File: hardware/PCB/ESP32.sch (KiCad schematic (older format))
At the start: 24 parts, among them IC5 ESP32-D0WD-V3, U3 ESP32_Antenna, Y1 ABS05-32.768KHZ-T, Y2 ABM11AIG-40.000MHZ-4-1Z-T

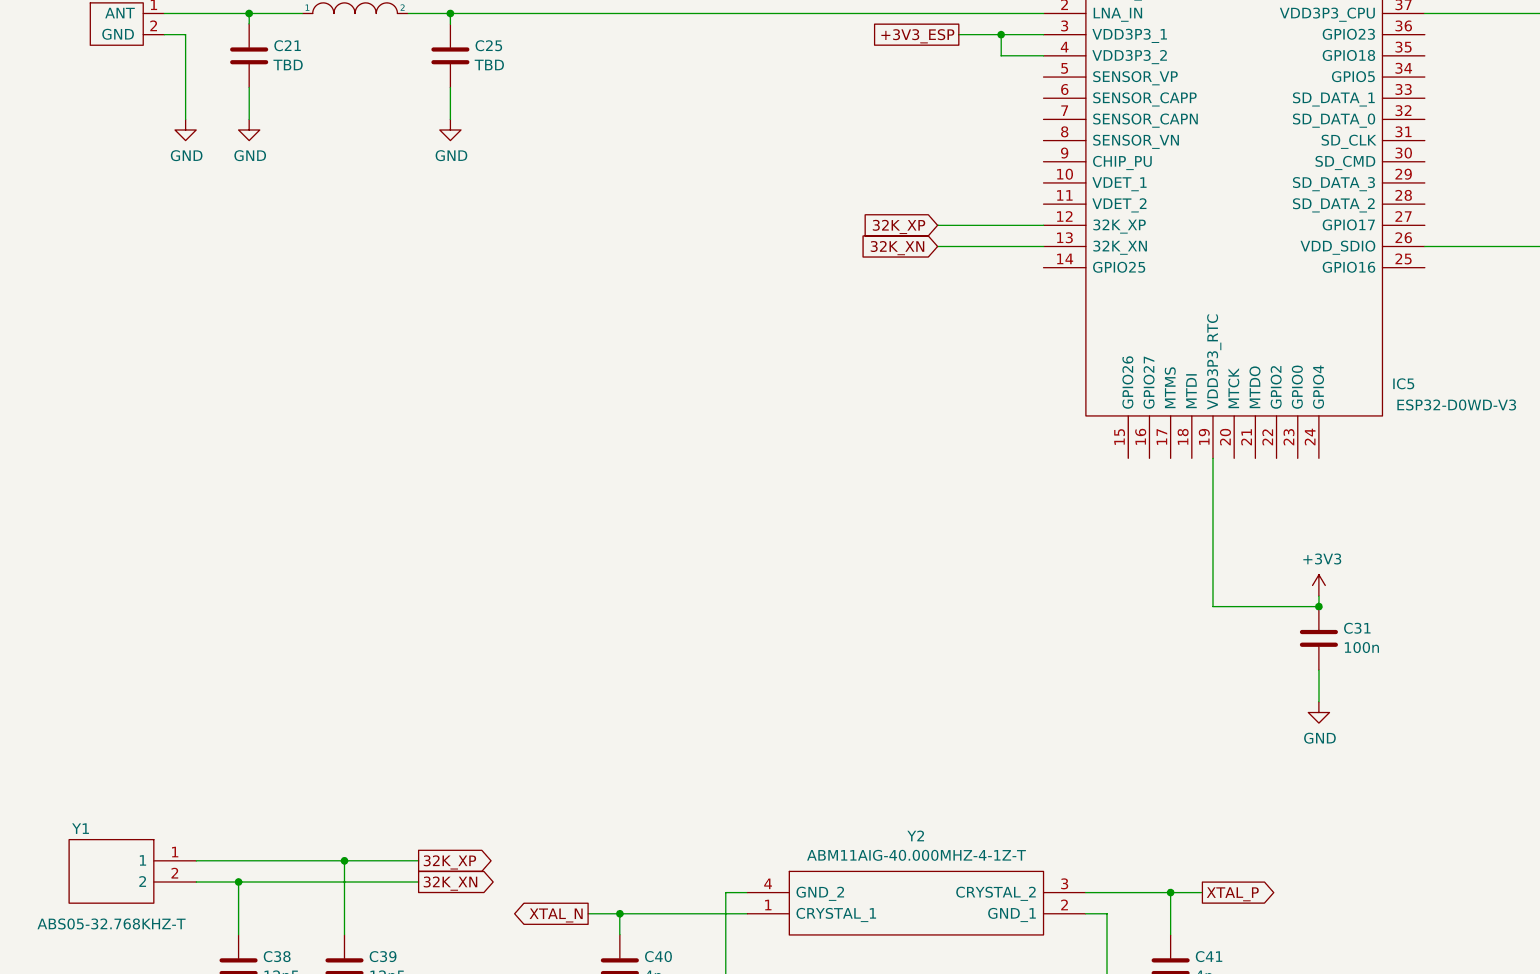
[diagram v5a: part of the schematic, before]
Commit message: add ESP32 bootloader circuit
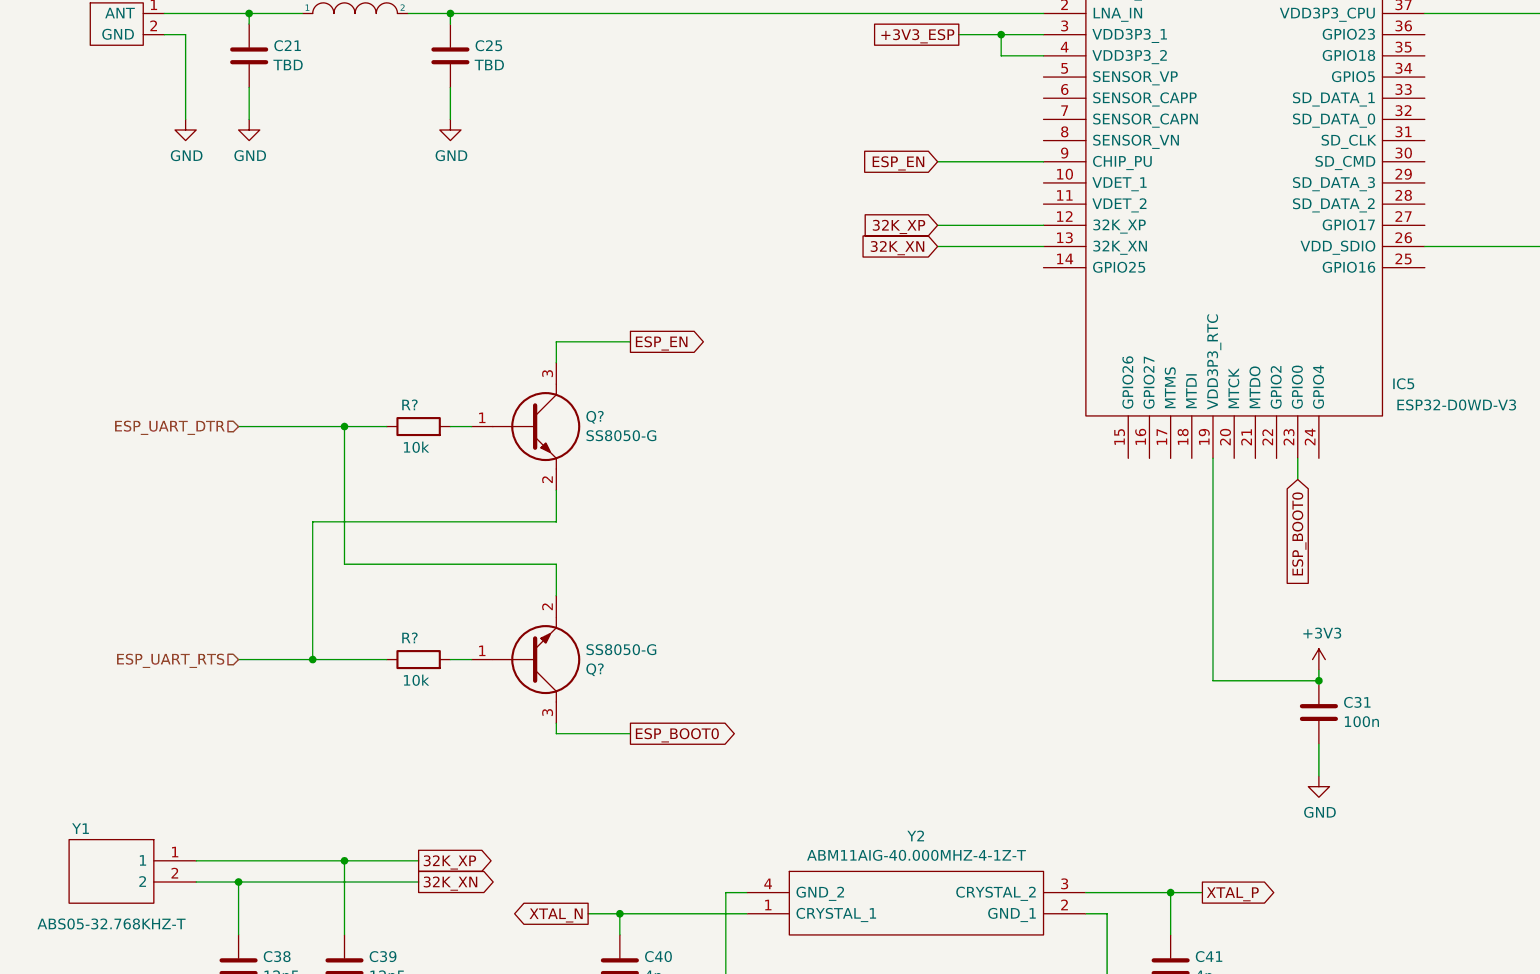
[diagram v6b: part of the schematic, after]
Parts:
- added Q? (x2): SS8050-G, SOT95P240X115-3N, symbol ProjectLibrary:SS8050-G
- added R? (x2): 10k, Resistor_SMD:R_0603_1608Metric, symbol Device:R
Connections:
- net ESP_BOOT0: now reaches IC5.23 (GPIO0)
- net ESP_BOOT0: now also Q?.3
- net ESP_EN: now reaches IC5.9 (CHIP_PU)
- net ESP_EN: now also Q?.3
- new net: Q?.1, R?.2 (x2)
- new net ESP_UART_DTR: Q?.2, R?.1
- new net ESP_UART_RTS: Q?.2, R?.1
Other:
- moved on the sheet: C31
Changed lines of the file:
@@
 L Device:C C?
 U 1 1 5FD526EC
-P 6600 5700
+P 6600 6050
 AR Path="/5FD526EC" Ref="C?"  Part="1"
 AR Path="/5FCFD0E2/5FD526EC" Ref="C31"  Part="1"
 AR Path="/5FE895CA/5FD526EC" Ref="C?"  Part="1"
-F 0 "C31" H 6715 5746 50  0000 L CNN
-F 1 "100n" H 6715 5655 50  0000 L CNN
-F 2 "Capacitor_SMD:C_0603_1608Metric" H 6638 5550 50  0001 C CNN
-F 3 "~" H 6600 5700 50  0001 C CNN
-	1    6600 5700
+F 0 "C31" H 6715 6096 50  0000 L CNN
+F 1 "100n" H 6715 6005 50  0000 L CNN
+F 2 "Capacitor_SMD:C_0603_1608Metric" H 6638 5900 50  0001 C CNN
+F 3 "~" H 6600 6050 50  0001 C CNN
+	1    6600 6050
 	1    0    0    -1
 $EndComp
@@
 L power:GND #PWR?
 U 1 1 5FD526F2
-P 6600 6000
+P 6600 6350
 AR Path="/5FD526F2" Ref="#PWR?"  Part="1"
 AR Path="/5FCFD0E2/5FD526F2" Ref="#PWR071"  Part="1"
 AR Path="/5FE895CA/5FD526F2" Ref="#PWR?"  Part="1"
-F 0 "#PWR071" H 6600 5750 50  0001 C CNN
-F 1 "GND" H 6605 5827 50  0000 C CNN
-F 2 "" H 6600 6000 50  0001 C CNN
-F 3 "" H 6600 6000 50  0001 C CNN
-	1    6600 6000
-	1    0    0    -1
-$EndComp
-Wire Wire Line
-	6600 5850 6600 6000
-Wire Wire Line
-	6100 4850 6100 5550
-Wire Wire Line
-	6100 5550 6600 5550
+F 0 "#PWR071" H 6600 6100 50  0001 C CNN
+F 1 "GND" H 6605 6177 50  0000 C CNN
+F 2 "" H 6600 6350 50  0001 C CNN
+F 3 "" H 6600 6350 50  0001 C CNN
+	1    6600 6350
+	1    0    0    -1
+$EndComp
+Wire Wire Line
+	6600 6200 6600 6350
+Wire Wire Line
+	6100 5900 6600 5900
 $Comp
 L ABS05-32.768KHZ-T:ABS05-32.768KHZ-T Y1
@@
 L power:+3V3 #PWR093
 U 1 1 5FF8D277
-P 6600 5500
+P 6600 5850
 AR Path="/5FCFD0E2/5FF8D277" Ref="#PWR093"  Part="1"
 AR Path="/5FE895CA/5FF8D277" Ref="#PWR?"  Part="1"
-F 0 "#PWR093" H 6600 5350 50  0001 C CNN
-F 1 "+3V3" H 6615 5673 50  0000 C CNN
-F 2 "" H 6600 5500 50  0001 C CNN
-F 3 "" H 6600 5500 50  0001 C CNN
-	1    6600 5500
-	1    0    0    -1
-$EndComp
-Wire Wire Line
-	6600 5500 6600 5550
-Connection ~ 6600 5550
+F 0 "#PWR093" H 6600 5700 50  0001 C CNN
+F 1 "+3V3" H 6615 6023 50  0000 C CNN
+F 2 "" H 6600 5850 50  0001 C CNN
+F 3 "" H 6600 5850 50  0001 C CNN
+	1    6600 5850
+	1    0    0    -1
+$EndComp
+Wire Wire Line
+	6600 5850 6600 5900
+Connection ~ 6600 5900
 $Comp
 L ProjectLibrary:ABM11AIG-40.000MHZ-4-1Z-T Y2
@@
 Wire Wire Line
 	6100 1800 6100 1950
+$Comp
+L ProjectLibrary:SS8050-G Q?
+U 1 1 5FFFFA03
+P 2600 4700
+F 0 "Q?" H 3138 4746 50  0000 L CNN
+F 1 "SS8050-G" H 3138 4655 50  0000 L CNN
+F 2 "SOT95P240X115-3N" H 3150 4550 50  0001 L CNN
+F 3 "http://www.comchiptech.com/admin/files/product/SS8050-G%20RevA181526.pdf" H 3150 4450 50  0001 L CNN
+F 4 "Bipolar Transistors - BJT NPN TRANSISTOR 1.5A 40V" H 3150 4350 50  0001 L CNN "Description"
+F 5 "1.15" H 3150 4250 50  0001 L CNN "Height"
+F 6 "750-SS8050-G" H 3150 4150 50  0001 L CNN "Mouser Part Number"
+F 7 "https://www.mouser.co.uk/ProductDetail/Comchip-Technology/SS8050-G/?qs=LLUE9lz1YbcHg%252BWLMAtcrQ%3D%3D" H 3150 4050 50  0001 L CNN "Mouser Price/Stock"
+F 8 "Comchip Technology" H 3150 3950 50  0001 L CNN "Manufacturer_Name"
+F 9 "SS8050-G" H 3150 3850 50  0001 L CNN "Manufacturer_Part_Number"
+	1    2600 4700
+	1    0    0    -1
+$EndComp
+$Comp
+L ProjectLibrary:SS8050-G Q?
+U 1 1 60008ECC
+P 2600 5800
+F 0 "Q?" H 3138 5846 50  0000 L CNN
+F 1 "SS8050-G" H 3138 5755 50  0000 L CNN
+F 2 "SOT95P240X115-3N" H 3150 5650 50  0001 L CNN
+F 3 "http://www.comchiptech.com/admin/files/product/SS8050-G%20RevA181526.pdf" H 3150 5550 50  0001 L CNN
+F 4 "Bipolar Transistors - BJT NPN TRANSISTOR 1.5A 40V" H 3150 5450 50  0001 L CNN "Description"
+F 5 "1.15" H 3150 5350 50  0001 L CNN "Height"
+F 6 "750-SS8050-G" H 3150 5250 50  0001 L CNN "Mouser Part Number"
+F 7 "https://www.mouser.co.uk/ProductDetail/Comchip-Technology/SS8050-G/?qs=LLUE9lz1YbcHg%252BWLMAtcrQ%3D%3D" H 3150 5150 50  0001 L CNN "Mouser Price/Stock"
+F 8 "Comchip Technology" H 3150 5050 50  0001 L CNN "Manufacturer_Name"
+F 9 "SS8050-G" H 3150 4950 50  0001 L CNN "Manufacturer_Part_Number"
+	1    2600 5800
+	1    0    0    1
+$EndComp
+$Comp
+L Device:R R?
+U 1 1 6000F441
+P 2350 4700
+AR Path="/6000F441" Ref="R?"  Part="1"
+AR Path="/5FCFD0E2/6000F441" Ref="R?"  Part="1"
+AR Path="/5FE895CA/6000F441" Ref="R?"  Part="1"
+F 0 "R?" V 2450 4700 50  0000 L CNN
+F 1 "10k" V 2250 4650 50  0000 L CNN
+F 2 "Resistor_SMD:R_0603_1608Metric" V 2280 4700 50  0001 C CNN
+F 3 "~" H 2350 4700 50  0001 C CNN
+	1    2350 4700
+	0    -1   -1   0
+$EndComp
+$Comp
+L Device:R R?
+U 1 1 60013917
+P 2350 5800
+AR Path="/60013917" Ref="R?"  Part="1"
+AR Path="/5FCFD0E2/60013917" Ref="R?"  Part="1"
+AR Path="/5FE895CA/60013917" Ref="R?"  Part="1"
+F 0 "R?" V 2450 5800 50  0000 L CNN
+F 1 "10k" V 2250 5750 50  0000 L CNN
+F 2 "Resistor_SMD:R_0603_1608Metric" V 2280 5800 50  0001 C CNN
+F 3 "~" H 2350 5800 50  0001 C CNN
+	1    2350 5800
+	0    -1   -1   0
+$EndComp
+Text HLabel 1500 5800 0    50   Input ~ 0
+ESP_UART_RTS
+Text HLabel 1500 4700 0    50   Input ~ 0
+ESP_UART_DTR
+Wire Wire Line
+	2500 4700 2600 4700
+Wire Wire Line
+	2500 5800 2600 5800
+Wire Wire Line
+	1500 4700 2000 4700
+Wire Wire Line
+	1500 5800 1850 5800
+Wire Wire Line
+	3000 5500 3000 5350
+Wire Wire Line
+	3000 5350 2000 5350
+Wire Wire Line
+	2000 5350 2000 4700
+Connection ~ 2000 4700
+Wire Wire Line
+	2000 4700 2200 4700
+Wire Wire Line
+	3000 5000 3000 5150
+Wire Wire Line
+	3000 5150 1850 5150
+Wire Wire Line
+	1850 5150 1850 5800
+Connection ~ 1850 5800
+Wire Wire Line
+	1850 5800 2200 5800
+Text GLabel 3350 4300 2    50   Output ~ 0
+ESP_EN
+Wire Wire Line
+	3000 4400 3000 4300
+Wire Wire Line
+	3000 4300 3350 4300
+Text GLabel 3350 6150 2    50   Output ~ 0
+ESP_BOOT0
+Wire Wire Line
+	3350 6150 3000 6150
+Wire Wire Line
+	3000 6150 3000 6100
+Text GLabel 6500 4950 3    50   Input ~ 0
+ESP_BOOT0
+Wire Wire Line
+	6100 4850 6100 5900
+Wire Wire Line
+	6500 4950 6500 4850
+Text GLabel 4800 3450 0    50   Input ~ 0
+ESP_EN
+Wire Wire Line
+	4800 3450 5300 3450
 $EndSCHEMATC

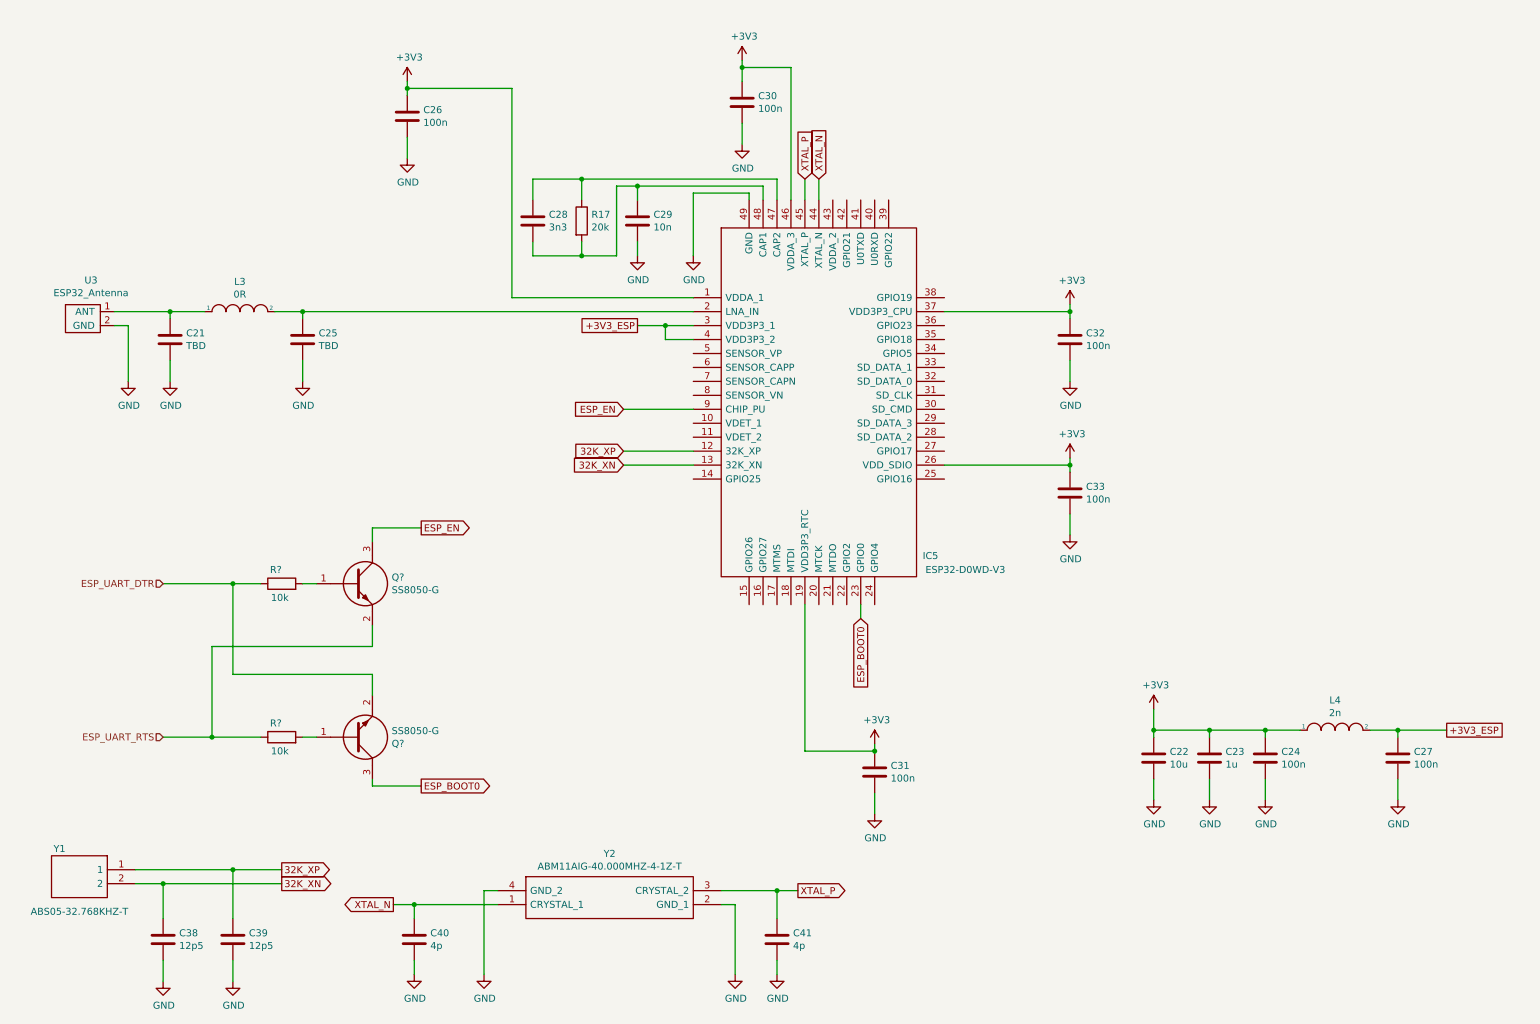
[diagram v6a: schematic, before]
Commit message: add enable and boot0 buttons
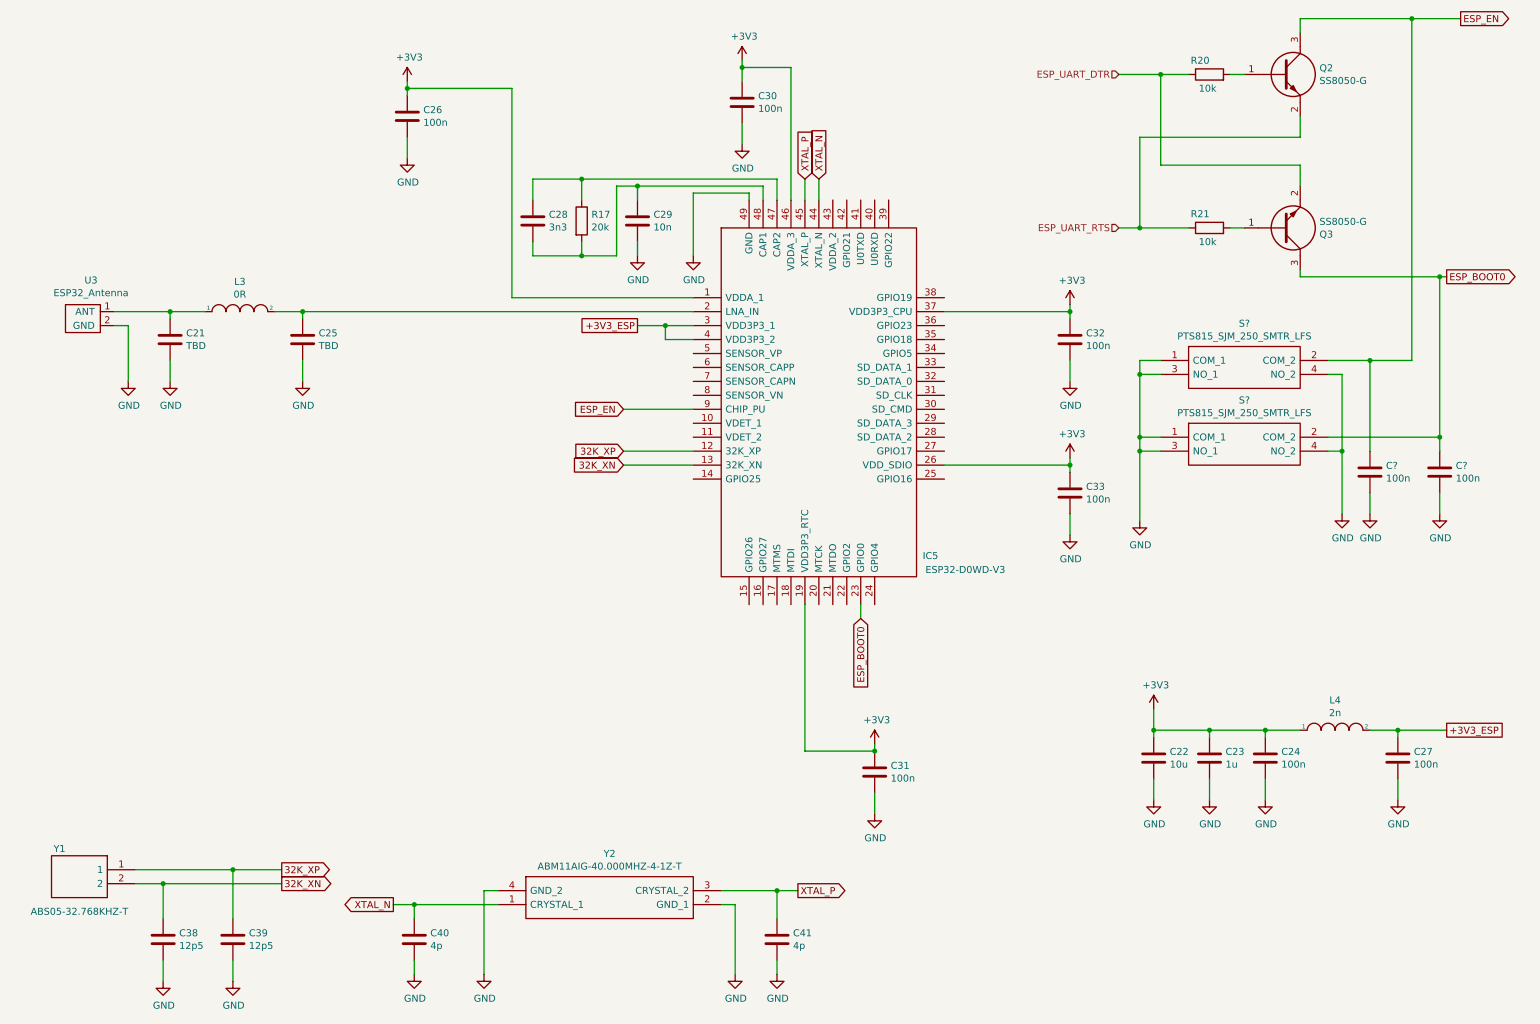
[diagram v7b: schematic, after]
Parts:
- added C? (x2): 100n, Capacitor_SMD:C_0603_1608Metric, symbol Device:C
- added S? (x2): PTS815_SJM_250_SMTR_LFS, PTS815SJM250SMTRLFS, symbol ProjectLibrary:PTS815_SJM_250_SMTR_LFS
- gave numbers to parts that had none: 4
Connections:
- net ESP_BOOT0: now also C?.1, S?.2 (COM_2)
- net ESP_EN: now also C?.1, S?.2 (COM_2)
- net GND: now also C?.2, C?.2, S?.1 (COM_1), S?.1 (COM_1), S?.3 (NO_1), S?.3 (NO_1), S?.4 (NO_2), S?.4 (NO_2)
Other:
- moved on the sheet: Q2, Q3, R20, R21
